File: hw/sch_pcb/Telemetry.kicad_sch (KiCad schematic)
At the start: 31 parts, among them J13 HEADER_2x02_PARALLEL, J23 MCX, U11 SX1262, U12 PE4259, Y3 32MHz

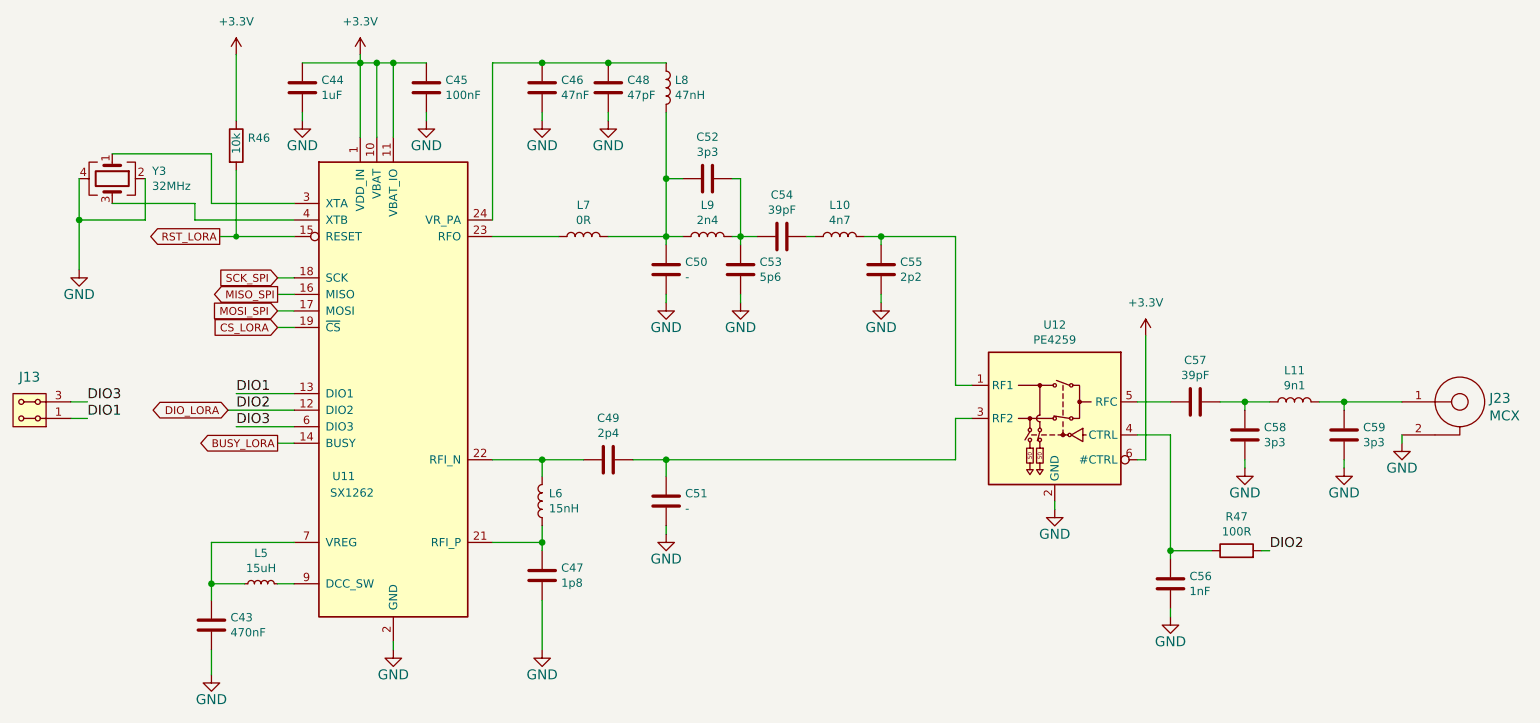
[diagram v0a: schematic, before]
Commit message: Update project to KiCADv9.
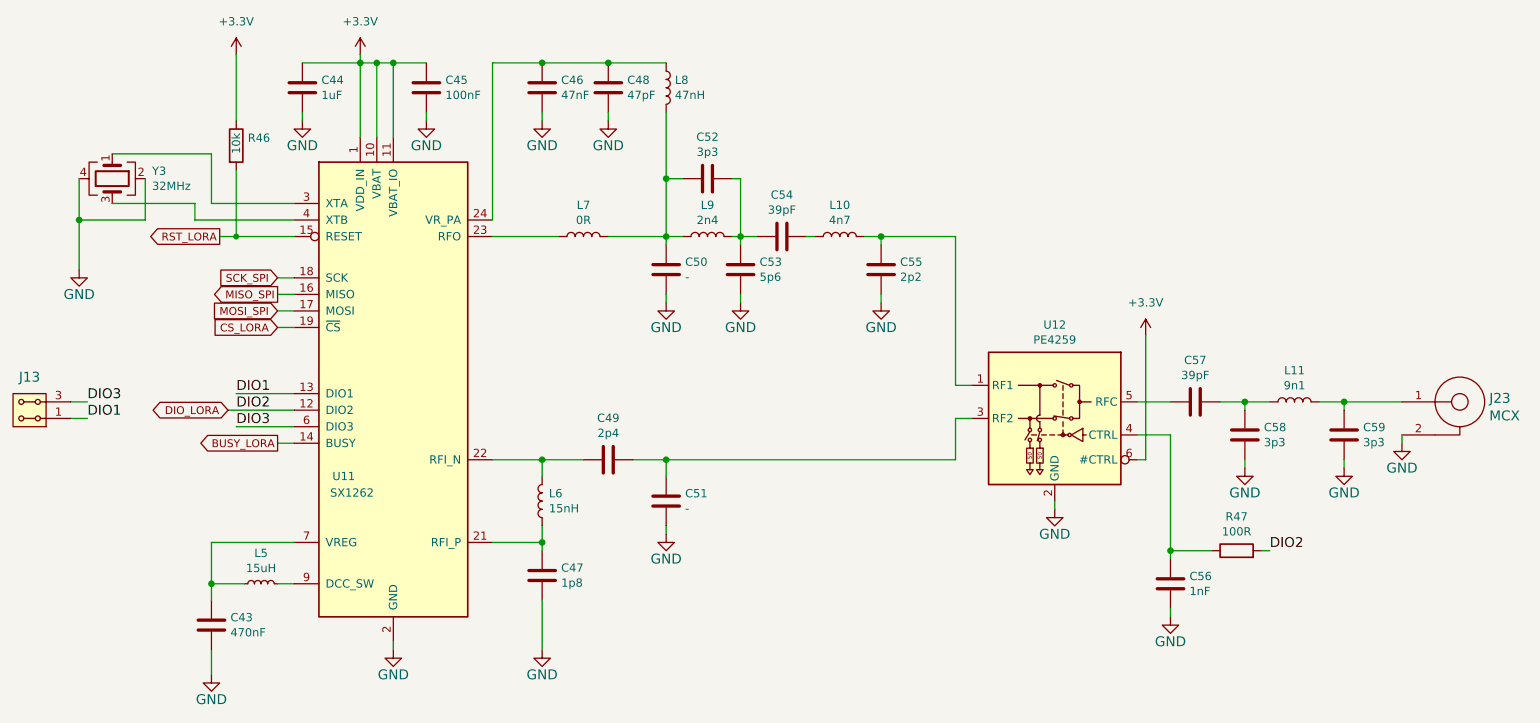
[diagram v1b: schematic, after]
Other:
- title: (none) -> DATALOGGER02A
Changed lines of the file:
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@@
 (kicad_sch
-	(version 20231120)
+	(version 20250114)
 	(generator "eeschema")
-	(generator_version "8.0")
+	(generator_version "9.0")
 	(paper "A4")
 	(title_block
+		(title "DATALOGGER02A")
 		(comment 3 "jacho <jacho@mlab.cz>")
 	)
